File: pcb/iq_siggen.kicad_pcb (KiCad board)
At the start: 4 copper layers, 100 x 100 mm, 255 parts, among them J1 J3 - BANK0, J10 Barrel_Jack, J11 Conn_Coaxial, J12 Conn_01x01_Male, J13 Conn_01x01_Male, J14 Conn_01x01_Male, J15 Conn_01x01_Male, J16 Conn_01x01_Male, J17 Conn_01x01_Male, J18 Conn_Coaxial, J19 Conn_Coaxial, J2 J4 - BANK1, J3 Conn_01x20_Male, J4 Conn_01x01_Male, J6 Conn_Coaxial, J7 Conn_Coaxial, J8 Conn_Coaxial, J9 Conn_Coaxial, SW1 SW_Push, SW2 SW_Push, T1 Transformer_1P_SS, T2 Transformer_1P_SS, T3 Transformer_1P_SS, T4 Transformer_1P_SS, U1 AMS1117-3.3, U2 TPS72325DBVR, U3 TLV73325PDBVT, U4 TLV3542IDR, U5 LM2596S-ADJ, U6 MAX5853ETL-T, U7 TLV3542IDR

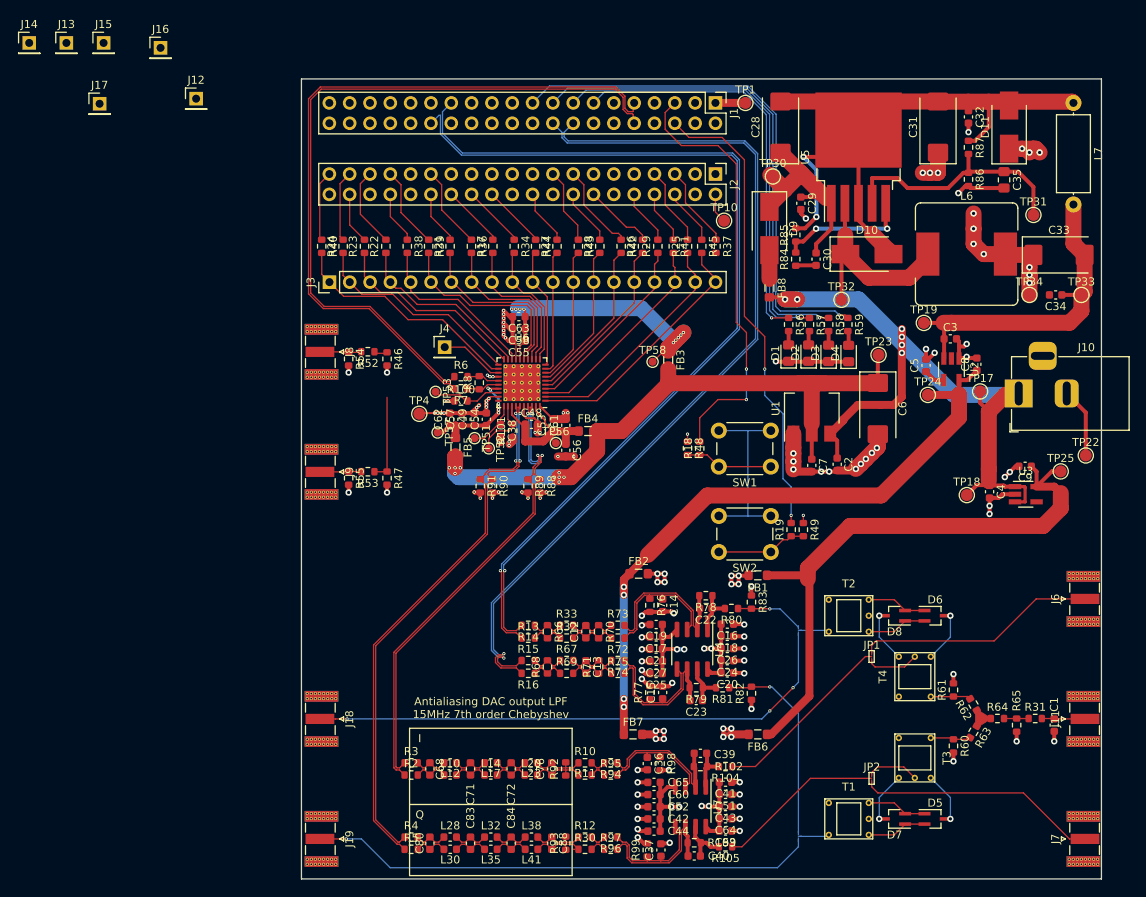
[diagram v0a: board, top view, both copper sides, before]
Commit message: layout refininements, stitching vias
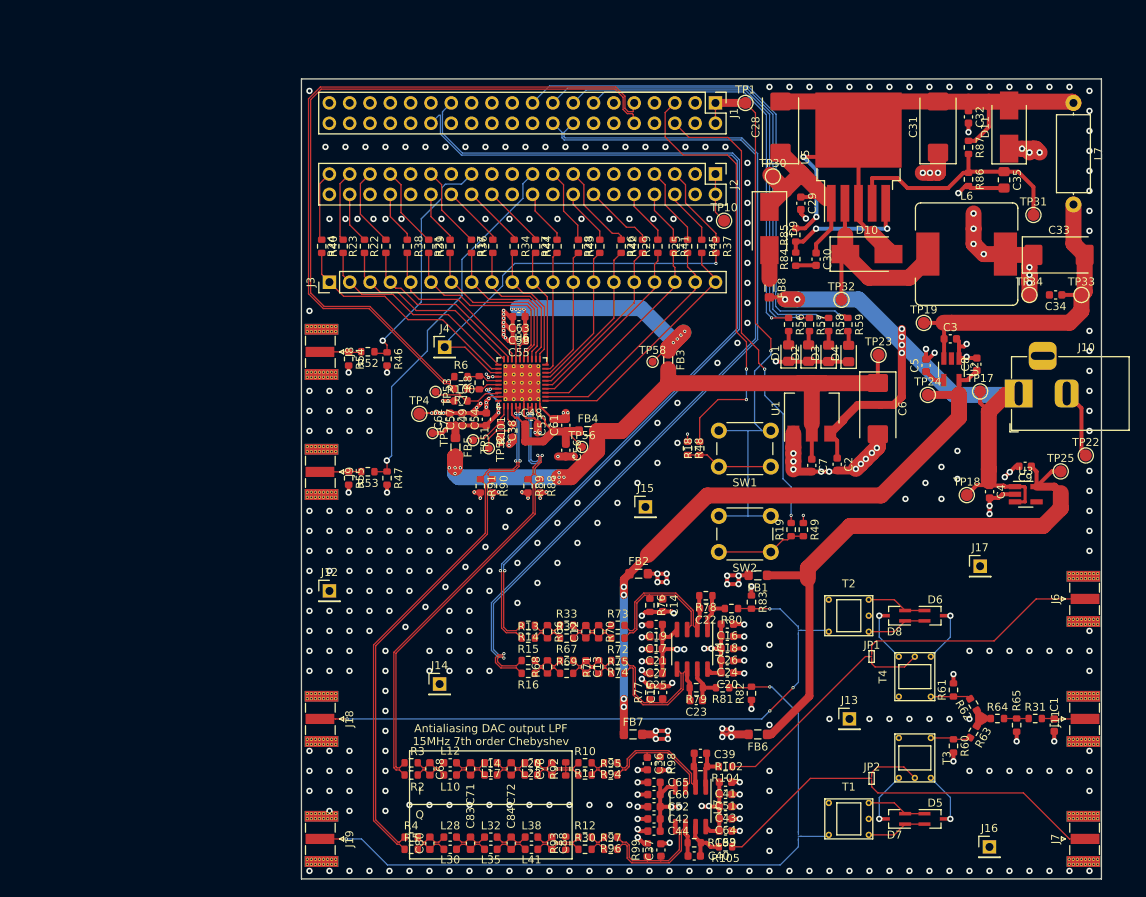
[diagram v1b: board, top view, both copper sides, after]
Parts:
- moved J16 143.9 mm to (136.0, 146.0)
- moved J13 129.3 mm to (118.5, 130.0)
- moved J17 124.3 mm to (134.8, 110.9)
- moved J14 95.2 mm to (67.3, 125.6)
- moved J15 89.2 mm to (93.0, 103.5)
- moved J12 63.7 mm to (53.5, 114.0)
- moved TP56 3.32 mm to (85.1, 96.0)
- moved TP57 0.64 mm to (66.4, 94.3)
- moved TP51 0.31 mm to (71.5, 95.2)
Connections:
- C49 pad 2: GNDS -> GNDA
- C54 pad 2: GNDS -> GNDA
- C55 pad 2: GNDD -> GNDA
- C57 pad 2: GNDS -> GNDA
- C58 pad 2: GNDD -> GNDA
- C62 pad 2: GNDS -> GNDA
- C63 pad 2: GNDD -> GNDA
- J1 pad 11: GNDS -> GNDA
- J1 pad 12: GNDS -> GNDA
- J2 pad 11: GNDD -> GNDA
- J2 pad 12: GNDD -> GNDA
- J2 pad 21: GNDD -> GNDA
- J2 pad 22: GNDD -> GNDA
- J2 pad 31: GNDD -> GNDA
- J2 pad 32: GNDD -> GNDA
- J8 pad 2: GNDD -> GNDA
- J9 pad 2: GNDD -> GNDA
- R100 pad 1: GNDS -> GNDA
- R46 pad 2: GNDD -> GNDA
- R47 pad 2: GNDD -> GNDA
- R54 pad 2: GNDD -> GNDA
- R55 pad 2: GNDD -> GNDA
- TP4 pad 1: GNDS -> GNDA
- U6 pad 17: GNDD -> GNDA
- U6 pad 24: GNDS -> GNDA
- U6 pad 29: GNDS -> GNDA
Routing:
- net /VCCIO0: track 27.4 -> 73.5 mm, vias 0 -> 1
- net GNDA: track 153.5 -> 195.4 mm, vias 89 -> 403
- net /~CW: track 8.04 -> 48.6 mm, vias 0 -> 1
- net /CLK_OUT: track 10.9 -> 46.3 mm, vias 0 -> 1
- net /CLK_EXT_IN: track 1.63 -> 29.9 mm, vias 0 -> 1
- net GNDD: track 16.6 -> 0.00 mm, vias 12 -> 0
- net GNDS: track 15.2 -> 0.00 mm, vias 15 -> 0
- net /VCCIO1: track 3.75 -> 6.29 mm
- net /IQ DAC and AA filter/AVDD: track 19.7 -> 21.8 mm
- net /IQ DAC and AA filter/CVDD: track 18.0 -> 19.3 mm, vias 6 -> 5
- net /IQ DAC and AA filter/-OPAMP_2.5V: track 16.5 -> 17.6 mm
- net /mixer/+OPAMP_2.5V: track 16.4 -> 17.4 mm
- net Net-(J1-Pad5): track 54.2 -> 54.8 mm
- net /IQ DAC and AA filter/DVDD: vias 9 -> 8
- net (no net): vias 0 -> 14
- removed copper zone on In1.Cu, net GNDD
- removed copper zone on In1.Cu, net GNDS
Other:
- rule trace_min: 0.0889 -> 0

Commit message: clean up designators on silkscreen, label connectors and circuit blocks
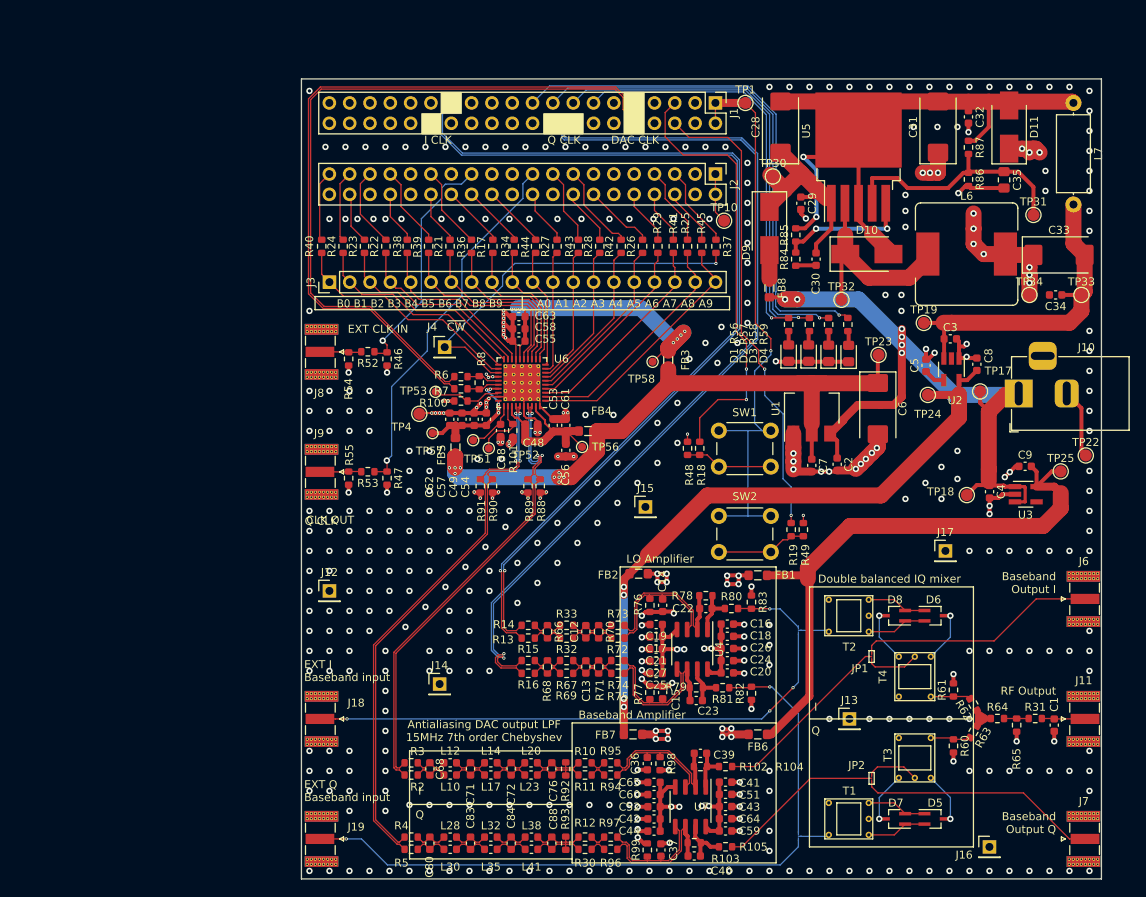
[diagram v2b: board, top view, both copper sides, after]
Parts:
- moved J17 4.74 mm to (130.5, 109.0)
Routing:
- net GNDA: vias 403 -> 445
- net (no net): vias 14 -> 0
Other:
- board text added: "A0 A1 A2 A3 A4 A5 A6 A7 A8 A9"
- board text added: "B0 B1 B2 B3 B4 B5 B6 B7 B8 B9"
- board text added: "Baseband Amplifier"
- board text added: "Baseband Output I"
- board text added: "Baseband Output Q"
- board text added: "CLK OUT"
- board text added: "DAC CLK"
- board text added: "Double balanced IQ mixer"
- board text added: "EXT CLK IN"
- board text added: "EXT I Baseband input"
- board text added: "EXT Q Baseband input"
- board text added: "I CLK"
- board text added: "LO Amplifier"
- board text added: "Q CLK"
- board text added: "RF Output"
- board text added: "~CW"

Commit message: clean up, label sub circuit blocks in silkscreen document the expected clock and baseband amplitudes based on opamp gains
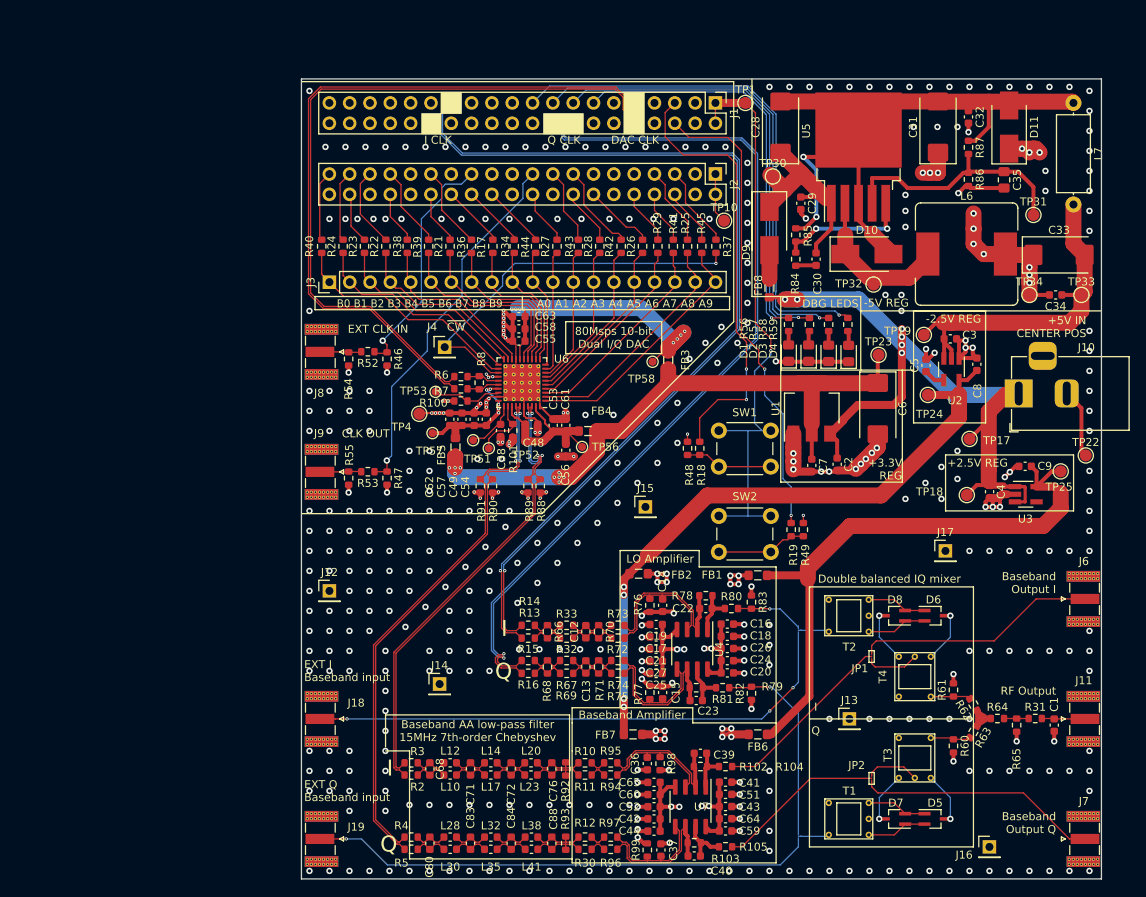
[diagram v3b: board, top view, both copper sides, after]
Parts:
- R76, R77, R78, R79: value 1k -> 1.5k
- moved TP17 6.08 mm to (133.5, 95.0)
- moved TP32 4.44 mm to (121.5, 75.7)
- moved TP19 1.50 mm to (127.8, 82.0)
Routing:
- net GNDA: track 195.4 -> 206.4 mm, vias 445 -> 452
- net Net-(D10-Pad1): track 24.8 -> 20.7 mm
- net -5V: track 41.7 -> 45.2 mm
- net +5V: track 88.1 -> 89.5 mm
- net /mixer/+OPAMP_2.5V: track 17.4 -> 16.4 mm
- net /IQ DAC and AA filter/-OPAMP_2.5V: track 17.6 -> 16.8 mm
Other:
- board text added: "+2.5V REG"
- board text added: "+3.3V REG"
- board text added: "+5V IN CENTER POS"
- board text added: "-2.5V REG"
- board text added: "-5V REG"
- board text added: "80Msps 10-bit Dual I/Q DAC"
- board text added: "Baseband AA low-pass filter 15MHz 7th-order Chebyshev"
- board text added: "DBG LEDS"
- board text removed: "Antialiasing DAC output LPF 15MHz 7th order Chebyshev"

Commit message: update the solder jumper clearance
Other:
- board text added: "GND"
- board text added: "Nebi Cicek 2020-12-10"
- board text added: "RF Signal Generator Add-On Board for Lattice MachXO3 FPGA Starter Kit"

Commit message: populate LCSC BOM for JLCPCB assembly
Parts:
- C14, C15, C22, C23, C36, C37, C39, C40: value 5p -> 4.7p
- C68, C76, C80, C88: value 85p -> 330p
- C71, C72, C83, C84: value 187p -> 680p
- L10, L12, L20, L23, L28, L30, L38, L41: value 732n -> 330n
- L14, L17, L32, L35: value 866n -> 470n
- R104, R105, R80, R81, R92, R93: value 50 -> 49.9
- R48, R49: value 10k -> 3k
- R62, R63, R64: value 16.666 -> 16.5
- R72, R73, R74, R75, R94, R95, R96, R97: value 500 -> 499
- R86: value 3.07k -> 3k
- R88, R89, R90, R91: value 25 -> 24.9

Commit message: add second parallel ferrite bead for input of negative 5V generator
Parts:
- added FB9: Ferrite_Bead_Small, Inductor_SMD:L_0805_2012Metric_Pad1.05x1.20mm_HandSolder, F.Cu at (110.3, 76.2)
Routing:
- net Net-(D9-Pad2): track 3.60 -> 5.41 mm

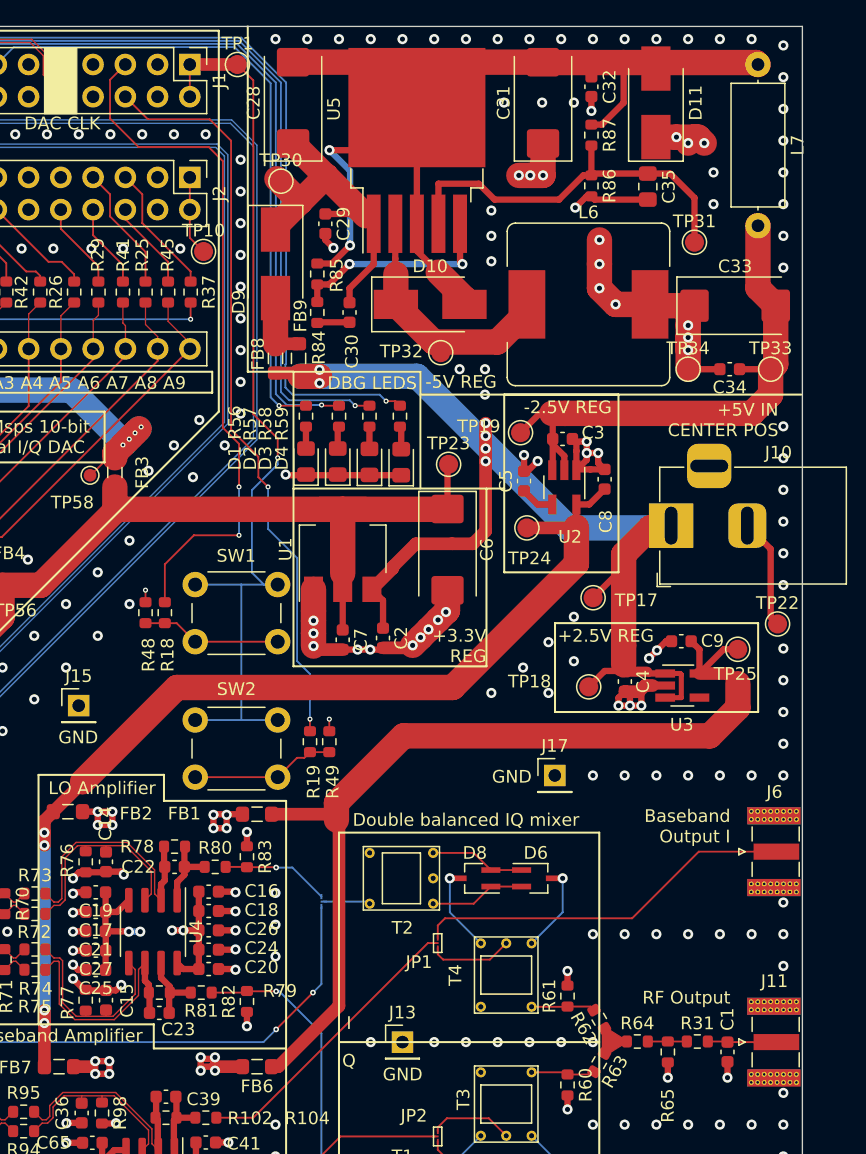
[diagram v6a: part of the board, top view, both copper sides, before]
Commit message: fill out more components in BOM with LCSC parts
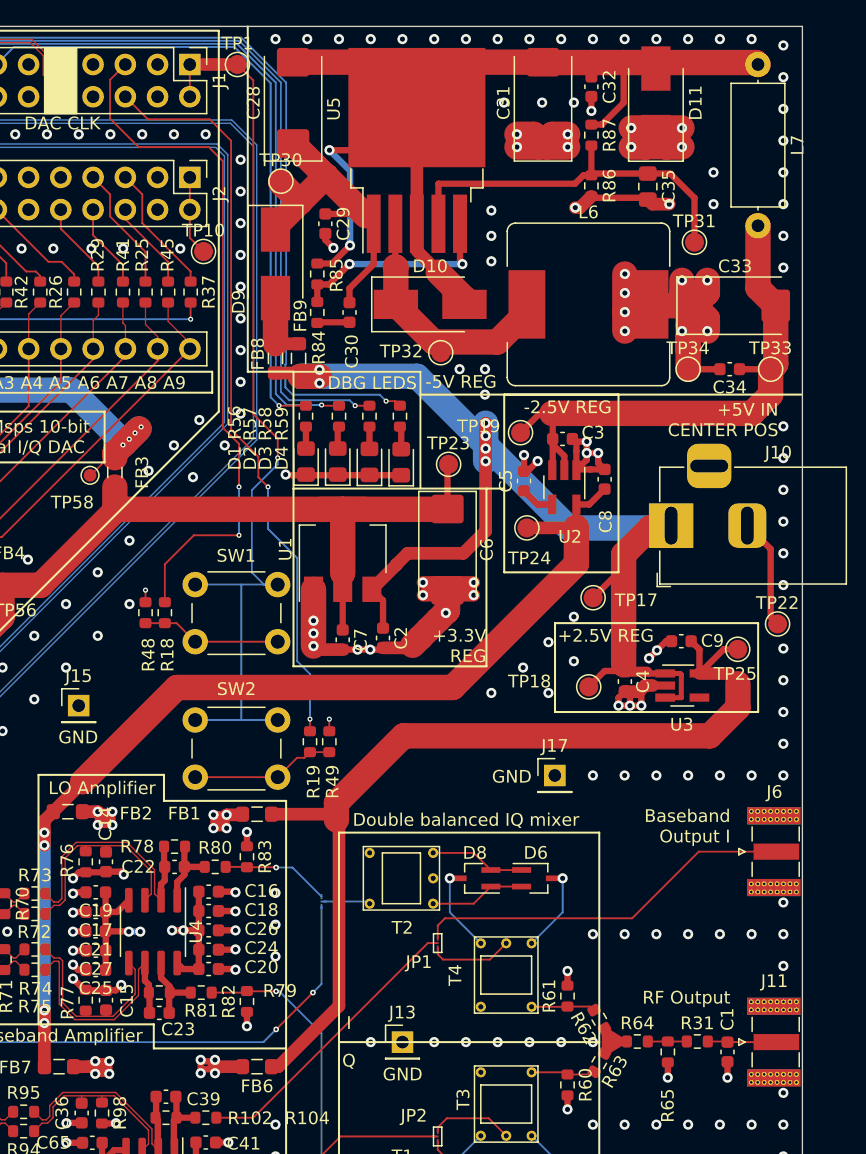
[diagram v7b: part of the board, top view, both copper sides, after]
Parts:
- C28, C31, C33, C6: footprint Capacitor_Tantalum_SMD:CP_EIA-7343-20_Kemet-V_Pad2.25x2.55mm_HandSolder -> Capacitor_Tantalum_SMD:CP_EIA-7343-43_Kemet-X_Pad2.25x2.55mm_HandSolder
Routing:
- net GNDA: track 206.4 -> 231.7 mm, vias 452 -> 456
- net +5V: track 89.6 -> 92.6 mm
- net /mixer/-OPAMP_2.5V: track 16.4 -> 18.7 mm
- net /mixer/+OPAMP_2.5V: track 16.4 -> 18.5 mm
- net /IQ DAC and AA filter/-OPAMP_2.5V: track 16.8 -> 18.0 mm
- net Net-(C35-Pad1): track 31.3 -> 30.3 mm
- net Net-(D10-Pad1): track 20.7 -> 21.3 mm
- net /IQ DAC and AA filter/+OPAMP_2.5V: track 16.2 -> 15.7 mm

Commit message: final touches
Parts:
- added G***: LOGO, iq_siggen:mooncake, F.Cu at (60.8, 109.0)
- moved R88 1.25 mm to (80.8, 101.6), turned to 0 degrees
- moved R90 1.08 mm to (74.6, 101.6), turned to 0 degrees
- moved R91 1.08 mm to (71.6, 101.6), turned to 180 degrees
- moved R89 0.94 mm to (77.8, 101.6), turned to 180 degrees
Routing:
- net GNDA: track 231.7 -> 341.7 mm, vias 456 -> 506
- net /IQ DAC and AA filter/+OPAMP_2.5V: track 15.7 -> 35.0 mm
- net /mixer/-OPAMP_2.5V: track 18.7 -> 37.4 mm
- net /mixer/+OPAMP_2.5V: track 18.5 -> 35.9 mm
- net /IQ DAC and AA filter/-OPAMP_2.5V: track 18.0 -> 35.1 mm
- net /mixer/LO_I_EXT: track 67.8 -> 73.9 mm
- net /mixer/IF_Q: track 6.58 -> 9.84 mm
- net /CLK_EXT_IN: track 29.9 -> 31.5 mm
- net /CLK_EXT_IN_Connector: track 5.24 -> 6.85 mm
- net /IQ DAC and AA filter/B_IOUT_N: track 67.1 -> 68.0 mm
- net +5V: track 92.6 -> 91.8 mm, vias 6 -> 7
- net /DAC_CLK_P: track 91.2 -> 90.5 mm
- net /negative rail generator/-5VO: track 85.7 -> 85.0 mm
- net /IQ DAC and AA filter/Q_DAC_OUT: track 20.8 -> 21.5 mm
- net /IQ DAC and AA filter/Q_FB_N: track 18.4 -> 17.8 mm
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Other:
- board text added: "Baseband AA low-pass filter 10MHz 7th-order Chebyshev"
- board text removed: "Baseband AA low-pass filter 15MHz 7th-order Chebyshev"
